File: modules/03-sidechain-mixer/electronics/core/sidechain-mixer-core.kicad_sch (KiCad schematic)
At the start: 8 parts, among them J1 Conn_01x04, J2 Conn_02x05_Odd_Even, J6 Conn_01x04, J8 Conn_01x06

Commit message: Mixer JLCPCB verified for 1.0
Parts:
- H1, H2, H3, H4, J1, J6: Vendor (none) -> Mouser
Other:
- company: (none) -> Shmøergh
- title: (none) -> Mixer & sidechain compressor
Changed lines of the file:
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@@
 	(generator_version "9.0")
 	(paper "A4")
+	(title_block
+		(title "Mixer & sidechain compressor")
+		(date "2025-12-11")
+		(company "Shmøergh")
+	)
 	(text "Power"
 		(exclude_from_sim no)
@@
 			)
 		)
-		(property "Vendor" ""
+		(property "Vendor" "Mouser"
 			(at 215.9 66.04 0)
 			(effects
@@
 			)
 		)
-		(property "Vendor" ""
+		(property "Vendor" "Mouser"
 			(at 200.66 160.02 0)
 			(effects
@@
 			)
 		)
-		(property "Vendor" ""
+		(property "Vendor" "Mouser"
 			(at 179.07 160.02 0)
 			(effects
@@
 			)
 		)
-		(property "Vendor" ""
+		(property "Vendor" "Mouser"
 			(at 220.98 160.02 0)
 			(effects
@@
 			)
 		)
-		(property "Vendor" ""
+		(property "Vendor" "Mouser"
 			(at 241.3 160.02 0)
 			(effects
@@
 			)
 		)
-		(property "Vendor" ""
+		(property "Vendor" "Mouser"
 			(at 215.9 83.82 0)
 			(effects

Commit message: Added full BOM to Mixer module
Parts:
- J1, J6: CHECKED (none) -> YES; Mouser Part no. (none) -> 200-HTSW10407TS; Part URL (none) -> https://mou.sr/3UfnMcJ
- J2: CHECKED (none) -> YES; Mouser Part no. (none) -> 200-HTSW10507TD; Part URL (none) -> https://mou.sr/3MXhCO3
- J8: CHECKED (none) -> YES; Mouser Part no. (none) -> 200-HTSW10607TS; Part URL (none) -> https://mou.sr/3YpdCIF
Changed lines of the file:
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@@
 			)
 		)
-		(property "Part URL" ""
+		(property "Part URL" "https://mou.sr/3UfnMcJ"
 			(at 215.9 66.04 0)
 			(effects
@@
 		)
 		(property "LCSC" ""
+			(at 215.9 66.04 0)
+			(effects
+				(font
+					(size 1.27 1.27)
+				)
+				(hide yes)
+			)
+		)
+		(property "CHECKED" "YES"
+			(at 215.9 66.04 0)
+			(effects
+				(font
+					(size 1.27 1.27)
+				)
+				(hide yes)
+			)
+		)
+		(property "Mouser Part no." "200-HTSW10407TS "
 			(at 215.9 66.04 0)
 			(effects
@@
 			)
 		)
-		(property "Part URL" ""
+		(property "Part URL" "https://mou.sr/3YpdCIF"
 			(at 215.9 45.72 0)
 			(effects
@@
 			)
 		)
-		(property "CHECKED" ""
+		(property "CHECKED" "YES"
 			(at 215.9 45.72 0)
 			(effects
@@
 			)
 		)
-		(property "Mouser Part no." ""
+		(property "Mouser Part no." "200-HTSW10607TS"
 			(at 215.9 45.72 0)
 			(effects
@@
 			)
 		)
-		(property "Part URL" ""
+		(property "Part URL" "https://mou.sr/3MXhCO3"
 			(at 215.9 106.68 0)
 			(effects
@@
 			)
 		)
-		(property "CHECKED" ""
+		(property "CHECKED" "YES"
 			(at 215.9 106.68 0)
 			(effects
@@
 			)
 		)
-		(property "Mouser Part no." ""
+		(property "Mouser Part no." "200-HTSW10507TD "
 			(at 215.9 106.68 0)
 			(effects
@@
 			)
 		)
-		(property "Part URL" ""
+		(property "Part URL" "https://mou.sr/3UfnMcJ"
 			(at 215.9 83.82 0)
 			(effects
@@
 			(at 215.9 83.82 0)
 			(effects
+				(font
+					(size 1.27 1.27)
+				)
+				(hide yes)
+			)
+		)
+		(property "CHECKED" "YES"
+			(at 215.9 83.82 0)
+			(effects
+				(font
+					(size 1.27 1.27)
+				)
+				(hide yes)
+			)
+		)
+		(property "Mouser Part no." "200-HTSW10407TS "
+			(at 215.9 83.82 0)
+			(effects

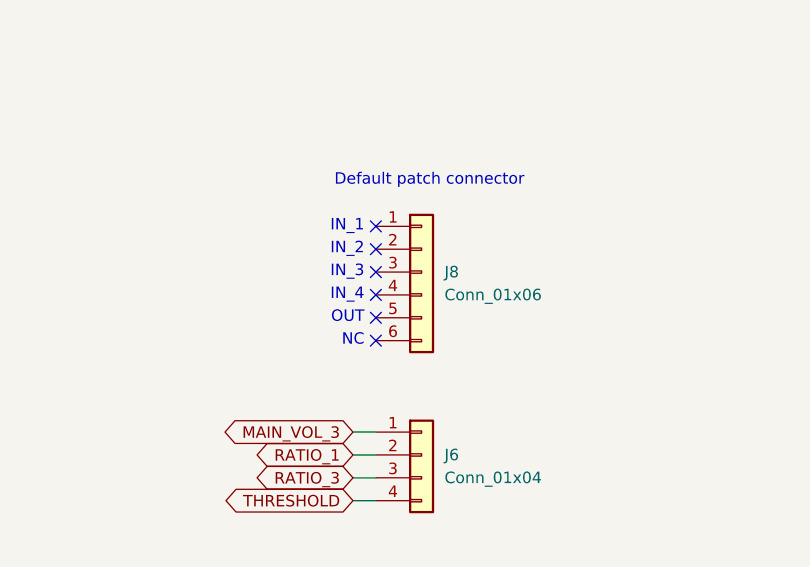
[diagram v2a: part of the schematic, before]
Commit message: Fixed socket to header on mixer UI
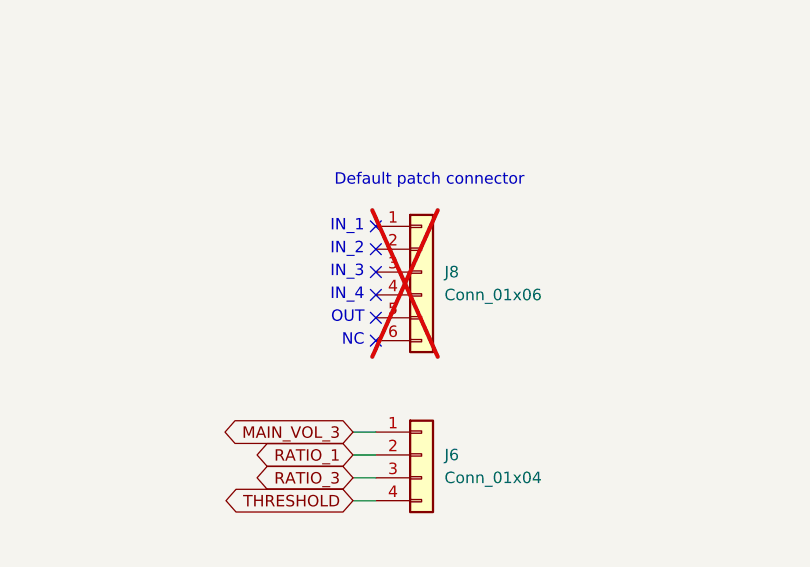
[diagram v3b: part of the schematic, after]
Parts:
- J8: now not fitted
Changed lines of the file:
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@@
 		(in_bom yes)
 		(on_board yes)
-		(dnp no)
+		(dnp yes)
 		(fields_autoplaced yes)
 		(property "Reference" "J8"
@@
 			(at 215.9 45.72 0)
 			(effects
+				(font
+					(size 1.27 1.27)
+				)
+				(hide yes)
+			)
+		)
+		(property "Part No." ""
+			(at 215.9 45.72 0)
+			(effects

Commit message: KiCAD version updates - PSU + VCO
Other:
- title: Mixer & sidechain compressor -> Moduleur Mixer & sidechain compressor
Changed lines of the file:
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@@
 	(paper "A4")
 	(title_block
-		(title "Mixer & sidechain compressor")
+		(title "Moduleur Mixer & sidechain compressor")
 		(date "2025-12-11")
+		(rev "v1.0")
 		(company "Shmøergh")
 	)
